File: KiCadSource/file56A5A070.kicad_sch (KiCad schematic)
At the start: 83 parts, among them U19 SPX3819, U20 MAX15053, U21 MAX15053, U22 MAX15053, U23 MCP4251, U24 LM2776, U25 MAX15053, U26 MAX15053, U27 SPX3819, U28 TPS72301

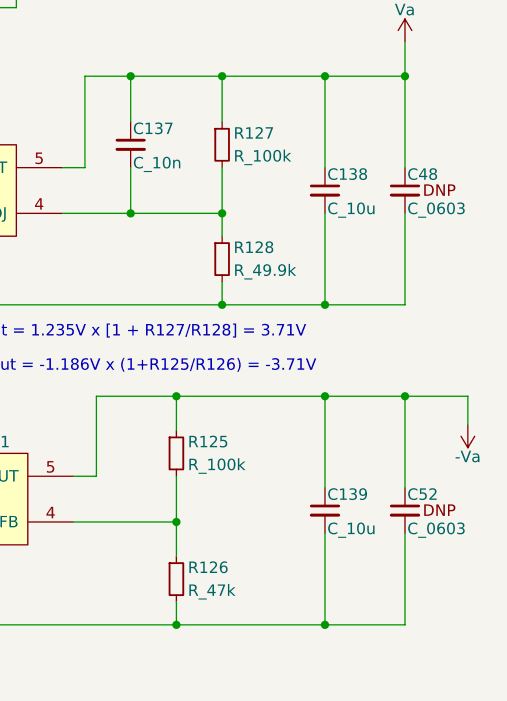
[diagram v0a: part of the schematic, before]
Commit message: updating part attributes
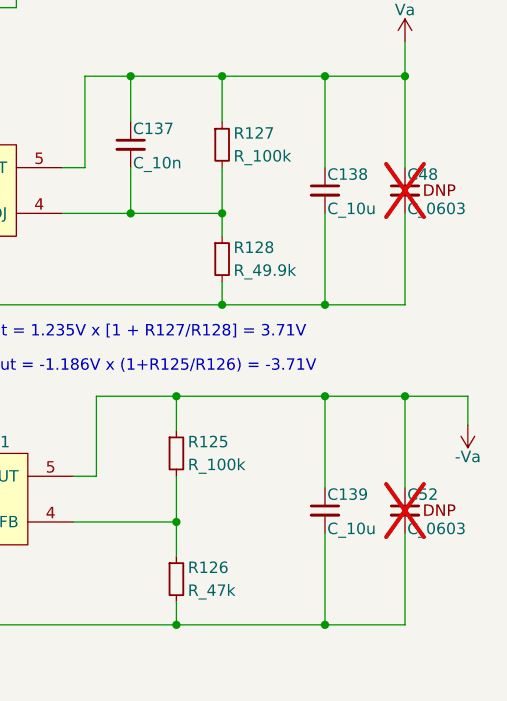
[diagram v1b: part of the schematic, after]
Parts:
- C48, C52: now not fitted
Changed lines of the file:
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@@
 		(in_bom yes)
 		(on_board yes)
-		(dnp no)
+		(dnp yes)
 		(property "Reference" "C48"
 			(at 272.034 97.282 0)
@@
 		(in_bom yes)
 		(on_board yes)
-		(dnp no)
+		(dnp yes)
 		(property "Reference" "C52"
 			(at 272.034 132.842 0)
